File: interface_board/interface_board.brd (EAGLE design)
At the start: 65 x 56 mm, 89 parts, among them IC1 V7805-1000, IC6 LAN9512-JZX, K2 61400826021, Q1 IRLML6346TRPBF, Q6 CTS_32X25_SMD, U1 AL5812MP-13, U2 MPU-9250

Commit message: after order
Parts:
- moved LOGO1 27.6 mm to (7.61, 33.7), turned to 90 degrees
- moved C1 5.94 mm to (17.7, 12.4), turned to 0 degrees
- moved FB2 3.52 mm to (34.6, 9.66), turned to 270 degrees
- moved C41 3.29 mm to (38.1, 3.43), turned to 270 degrees
- moved U1 3.05 mm to (16.4, 16.9)
- moved C16 2.41 mm to (17.7, 13.7)
- moved R8 2.29 mm to (51.7, 5.46), turned to 90 degrees
- moved R33 1.92 mm to (34.6, 13.2), turned to 90 degrees
- moved C29 1.71 mm to (47.2, 5.46)
- moved C35 1.53 mm to (38.4, 11.2), turned to 180 degrees
- moved C32 1.42 mm to (43.1, 11.7)
- moved C27 1.42 mm to (38.4, 7.24)
- moved C28 1.42 mm to (38.4, 9.78)
- moved C39 1.42 mm to (47.2, 2.79)
- moved C40 1.42 mm to (47.2, 4.06)
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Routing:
- net 3V3A: track 82.7 -> 104.2 mm
- net +3V3: track 214.5 -> 208.0 mm, vias 9 -> 10
- net VDD18PLL: track 29.8 -> 33.3 mm
- net N$10: track 94.7 -> 98.0 mm
- net TX_P: track 63.2 -> 60.1 mm
- net N$5: track 1.68 -> 4.73 mm
- net +12V: track 70.3 -> 67.6 mm
- net +5V: track 119.2 -> 121.7 mm
- net N$9: track 85.1 -> 87.4 mm
- net XI: track 31.0 -> 32.6 mm
- net XO: track 26.5 -> 27.9 mm
- net N$43: track 7.12 -> 8.53 mm
- net NSPD_LED: track 55.8 -> 57.2 mm
- net USBD3_N: track 10.7 -> 12.0 mm
- net USBD2_N: track 7.97 -> 9.34 mm
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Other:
- outline, holes or cut-outs redrawn

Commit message: bom
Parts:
- C3: device SparkFun-Capacitors:0603-CAP -> resistor:C0402
- C42: device resistor:C0603 -> resistor:C0402
- JP1: value M20-9990446 -> SSQ-108-03-G-D
- JP2, JP3: value M20-9980346 -> M20-9980345
- JP4: value (none) -> M20-9980345
- JP6: value USB-IDMICRO -> 10118192-0001LF
- Q6: value CTS_32X25_SMD -> FA-238 25.0000MB
- R1: value 4.99K -> 4.99k
- R18, R3: value 1K -> 1k
- R2: value 100K -> 100k
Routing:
- net N$4: track 4.73 -> 4.02 mm
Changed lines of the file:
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@@
 <attribute name="NAME" x="58.9" y="25.935" size="0.6096" layer="25" font="vector" ratio="10" rot="R90"/>
 </element>
-<element name="R1" library="resistor" package="R0402" value="4.99K" x="23.008" y="18.707" smashed="yes" rot="R270">
+<element name="R1" library="resistor" package="R0402" value="4.99k" x="23.008" y="18.707" smashed="yes" rot="R270">
 <attribute name="NAME" x="23.77" y="19.342" size="0.6096" layer="25" rot="R270"/>
 <attribute name="VALUE" x="21.103" y="19.342" size="1.016" layer="27" rot="R270" display="off"/>
@@
 <attribute name="VALUE" x="17.042" y="10.505" size="1.016" layer="27" display="off"/>
 </element>
-<element name="R2" library="resistor" package="R0402" value="100K" x="16.898" y="21.312" smashed="yes" rot="R90">
+<element name="R2" library="resistor" package="R0402" value="100k" x="16.898" y="21.312" smashed="yes" rot="R90">
 <attribute name="NAME" x="17.152" y="22.963" size="0.6096" layer="25" rot="R90"/>
 <attribute name="VALUE" x="18.803" y="20.677" size="1.016" layer="27" rot="R90" display="off"/>
 </element>
-<element name="R3" library="resistor" package="R0402" value="1K" x="15.628" y="21.312" smashed="yes" rot="R270">
+<element name="R3" library="resistor" package="R0402" value="1k" x="15.628" y="21.312" smashed="yes" rot="R270">
 <attribute name="NAME" x="15.882" y="22.963" size="0.6096" layer="25" rot="R90"/>
 <attribute name="VALUE" x="13.723" y="21.947" size="1.016" layer="27" rot="R270" display="off"/>
@@
 <element name="H3" library="holes" package="2,8-PAD" value="MOUNT-PAD-ROUND2.8" x="61.5" y="3.5" smashed="yes" rot="R180"/>
 <element name="H4" library="holes" package="2,8-PAD" value="MOUNT-PAD-ROUND2.8" x="3.5" y="3.5" smashed="yes" rot="R180"/>
-<element name="JP1" library="pinhead" package="2X08" value="M20-9990446" x="17.26" y="52.5" smashed="yes" rot="MR180">
+<element name="JP1" library="pinhead" package="2X08" value="SSQ-108-03-G-D" x="17.26" y="52.5" smashed="yes" rot="MR180">
 <attribute name="NAME" x="16.6758" y="49.6552" size="0.6096" layer="26" ratio="10" rot="MR180"/>
 <attribute name="VALUE" x="12.18" y="55.675" size="1.27" layer="28" rot="MR180" display="off"/>
@@
 <attribute name="VALUE" x="18.312" y="15.628" size="1.016" layer="27" rot="R180" display="off"/>
 </element>
-<element name="R18" library="resistor" package="R0402" value="1K" x="8.536" y="25.761" smashed="yes" rot="MR180">
+<element name="R18" library="resistor" package="R0402" value="1k" x="8.536" y="25.761" smashed="yes" rot="MR180">
 <attribute name="NAME" x="5.488" y="26.015" size="0.6096" layer="26" rot="MR180"/>
 <attribute name="VALUE" x="7.901" y="27.666" size="1.016" layer="28" rot="MR180" display="off"/>
@@
 <attribute name="VALUE" x="5.227" y="18.061" size="1.016" layer="28" rot="MR90" display="off"/>
 </element>
-<element name="JP2" library="pinhead" package="2X03" value="M20-9980346" x="15.343" y="32.886" smashed="yes" rot="MR180">
+<element name="JP2" library="pinhead" package="2X03" value="M20-9980345" x="15.343" y="32.886" smashed="yes" rot="MR180">
 <attribute name="NAME" x="14.708" y="37.712" size="0.6096" layer="26" ratio="10" rot="MR180"/>
 <attribute name="VALUE" x="11.533" y="39.871" size="1.016" layer="28" rot="MR180" display="off"/>
 </element>
-<element name="JP3" library="pinhead" package="2X03" value="M20-9980346" x="33.403" y="3.936" smashed="yes" rot="MR90">
+<element name="JP3" library="pinhead" package="2X03" value="M20-9980345" x="33.403" y="3.936" smashed="yes" rot="MR90">
 <attribute name="NAME" x="36.324" y="3.301" size="0.6096" layer="26" ratio="10" rot="MR90"/>
 <attribute name="VALUE" x="26.418" y="0.126" size="1.016" layer="28" rot="MR90" display="off"/>
@@
 <attribute name="VALUE" x="36.195" y="4.064" size="0.6096" layer="27" rot="R270" display="off"/>
 </element>
-<element name="C42" library="resistor" package="C0603" value="1u" x="48.133" y="18.923" smashed="yes" rot="R270">
+<element name="C42" library="resistor" package="C0402" value="1u" x="48.133" y="18.923" smashed="yes" rot="R270">
 <attribute name="NAME" x="47.879" y="21.971" size="0.6096" layer="25" rot="R270"/>
 <attribute name="VALUE" x="44.958" y="19.685" size="0.6096" layer="27" rot="R270"/>
@@
 <attribute name="VALUE" x="26.924" y="13.97" size="0.6096" layer="27" rot="R270" display="off"/>
 </element>
-<element name="Q6" library="raspi" package="CTS_32X25" value="CTS_32X25_SMD" x="31.75" y="13.208" smashed="yes" rot="R90">
+<element name="Q6" library="raspi" package="CTS_32X25" value="FA-238 25.0000MB" x="31.75" y="13.208" smashed="yes" rot="R90">
 <attribute name="NAME" x="33.652" y="12.27" size="0.6096" layer="25" rot="R90"/>
 <attribute name="VALUE" x="33.85" y="11.508" size="0.6096" layer="27" rot="R90" display="off"/>
@@
 <attribute name="VALUE" x="31.357" y="37.465" size="0.6096" layer="27" ratio="11" display="off"/>
 </element>
-<element name="C3" library="SparkFun-Capacitors" package="0603-CAP" value="1uF" x="36.449" y="37.973" smashed="yes" rot="R180">
+<element name="C3" library="resistor" package="C0402" value="1uF" x="36.449" y="37.973" smashed="yes" rot="R180">
 <attribute name="NAME" x="36.957" y="36.957" size="0.6096" layer="25" font="vector" rot="R180"/>
 <attribute name="VALUE" x="37.465" y="39.116" size="0.6096" layer="27" font="vector" rot="R180" display="off"/>
 </element>
-<element name="JP6" library="openblw" package="USB-MICRO" value="USB-IDMICRO" x="18.796" y="1.524" smashed="yes">
+<element name="JP6" library="openblw" package="USB-MICRO" value="10118192-0001LF" x="18.796" y="1.524" smashed="yes">
 <attribute name="PROD_ID" value="CONN-09505" x="18.796" y="1.524" size="1.778" layer="27" display="off"/>
 </element>
-<element name="JP4" library="pinhead" package="2X03" value="" x="54.09" y="52.5" smashed="yes">
+<element name="JP4" library="pinhead" package="2X03" value="M20-9980345" x="54.09" y="52.5" smashed="yes">
 <attribute name="NAME" x="50.788" y="49.452" size="0.6096" layer="25" ratio="10"/>
-<attribute name="VALUE" x="50.28" y="48.055" size="1.27" layer="27"/>
+<attribute name="VALUE" x="50.28" y="48.055" size="1.27" layer="27" display="off"/>
 </element>
 <element name="LED3" library="led" package="CHIP-LED0603" value="GREEN" x="26.035" y="6.096" smashed="yes" rot="R180">
@@
 <wire x1="33.274" y1="41.402" x2="33.227" y2="41.449" width="0.2" layer="1"/>
 <wire x1="33.227" y1="41.449" x2="33.227" y2="41.986" width="0.2" layer="1"/>
-<wire x1="48.133" y1="19.773" x2="49.453" y2="19.78" width="0.2" layer="1"/>
-<wire x1="49.453" y1="19.78" x2="49.657" y2="19.573" width="0.2" layer="1"/>
+<wire x1="48.133" y1="19.573" x2="49.584" y2="19.572" width="0.2" layer="1"/>
+<wire x1="49.584" y1="19.572" x2="49.657" y2="19.573" width="0.2" layer="1"/>
 <wire x1="32.43" y1="38.783" x2="32.43" y2="37.637" width="0.2" layer="1"/>
 <wire x1="32.43" y1="37.637" x2="32.385" y2="37.592" width="0.2" layer="1"/>
@@
 <contactref element="FB3" pad="2"/>
 <via x="46.946" y="13.203" extent="1-16" drill="0.3"/>
-<wire x1="48.133" y1="18.073" x2="48.58" y2="18.012" width="0.2" layer="1"/>
+<wire x1="48.133" y1="18.273" x2="48.199" y2="18.266" width="0.2" layer="1"/>
 <wire x1="48.199" y1="16.256" x2="48.133" y2="16.444" width="0.2" layer="1"/>
-<wire x1="48.133" y1="16.444" x2="48.133" y2="18.073" width="0.2" layer="1"/>
+<wire x1="48.133" y1="16.444" x2="48.133" y2="18.273" width="0.2" layer="1"/>
 <wire x1="46.946" y1="13.203" x2="46.946" y2="15.704" width="0.2" layer="1"/>
 <wire x1="46.946" y1="15.704" x2="47.498" y2="16.256" width="0.2" layer="1"/>
@@
 <contactref element="C3" pad="2"/>
 <contactref element="U2" pad="10"/>
-<wire x1="35.599" y1="37.973" x2="36.107" y2="37.758" width="0.254" layer="1"/>
-<wire x1="36.107" y1="37.758" x2="36.068" y2="37.719" width="0.4064" layer="1"/>
-<wire x1="36.068" y1="37.719" x2="33.147" y2="37.719" width="0.4064" layer="1"/>
+<wire x1="35.799" y1="37.973" x2="35.726" y2="37.758" width="0.254" layer="1"/>
+<wire x1="35.726" y1="37.758" x2="35.687" y2="37.719" width="0.4064" layer="1"/>
+<wire x1="35.687" y1="37.719" x2="33.147" y2="37.719" width="0.4064" layer="1"/>
 <wire x1="33.147" y1="37.719" x2="32.827" y2="38.039" width="0.254" layer="1"/>
 <wire x1="32.827" y1="38.039" x2="32.827" y2="38.786" width="0.254" layer="1"/>

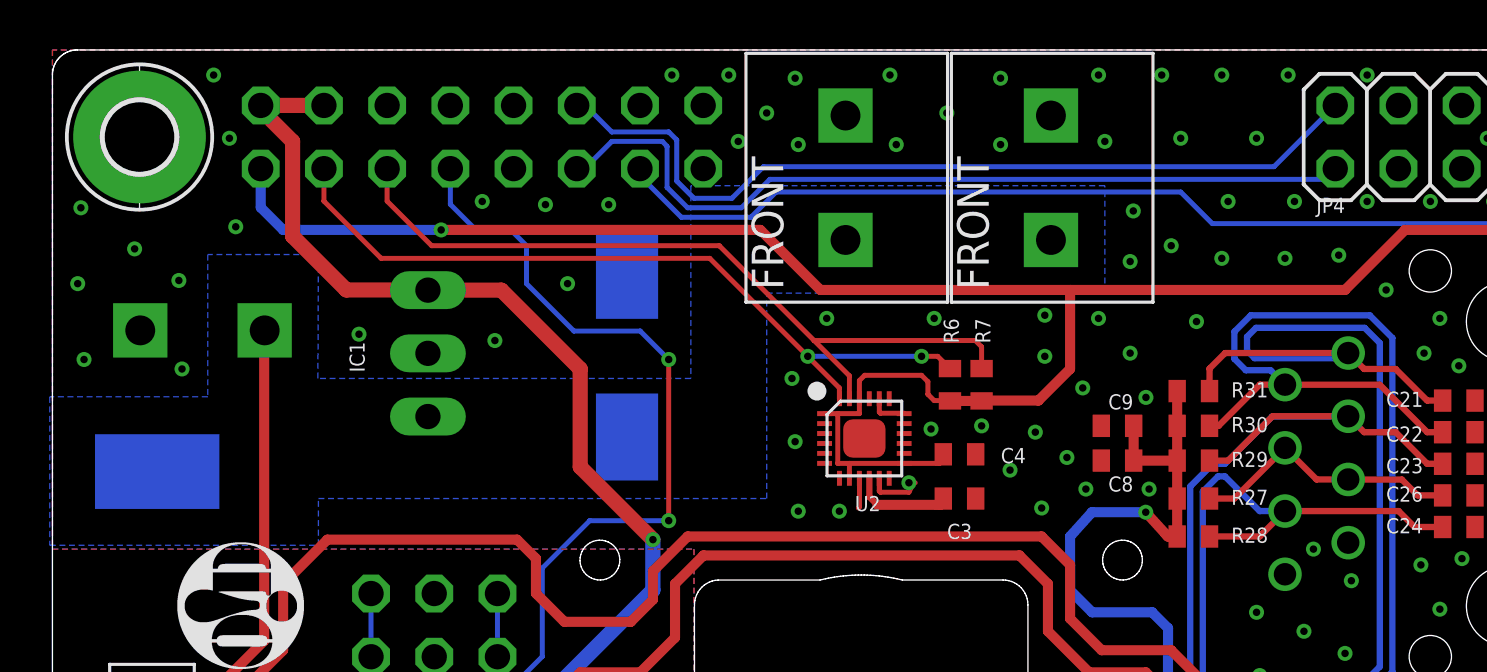
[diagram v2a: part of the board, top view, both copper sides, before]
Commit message: tune +5V
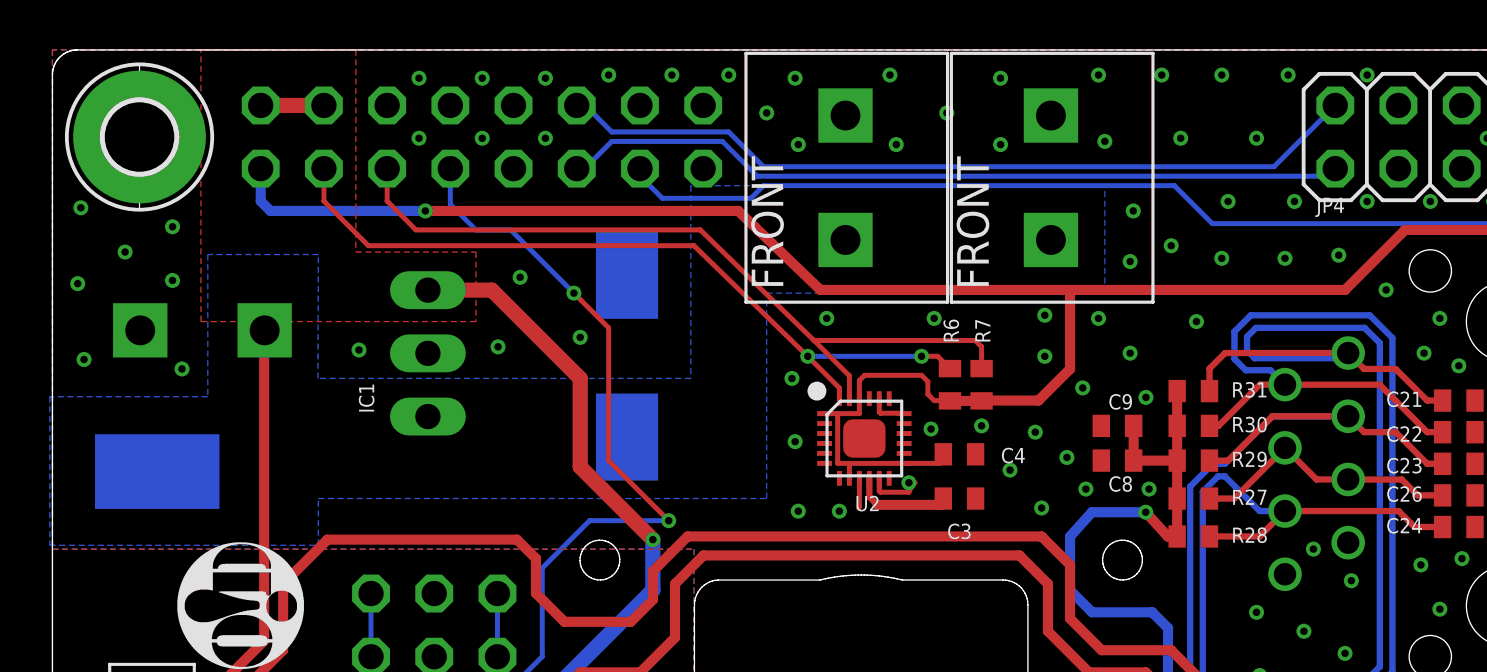
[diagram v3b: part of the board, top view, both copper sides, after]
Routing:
- net +5V: track 121.7 -> 109.3 mm
- net PWMA: track 33.7 -> 31.6 mm
- net PWMB: track 34.5 -> 32.5 mm
- net LIGHT_PWM: track 44.2 -> 42.6 mm
- net GND: vias 221 -> 223
- added copper zone on layer 1, net +5V

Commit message: before hdmi
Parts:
- removed R9: 10k, resistor:R0402
- removed U$7: 282836-2, openblw:282836-2
- added JP5: (no value), openblw:1X02
- JP1: device pinhead:2X08 -> pinhead:2X10
- R8: value 0 -> 12k
- moved JP6 56.2 mm to (37.6, 54.5), flipped to the bottom, turned to 180 degrees
- moved R8 55.1 mm to (-0.64, -11.9), turned to 0 degrees
- moved R7 39.3 mm to (21.7, 6.48)
- moved U2 38.8 mm to (18.3, 4.32)
- moved C3 38.8 mm to (22.1, 1.91)
- moved C4 38.8 mm to (22.1, 3.68)
- moved R6 38.4 mm to (23.0, 6.48)
- moved U$8 10.4 mm to (32.0, 40.4), turned to 0 degrees
- moved C17 8.86 mm to (4.09, 21.1), flipped to the top
- moved R18 5.44 mm to (4.09, 22.6), flipped to the top, turned to 0 degrees
- moved Q1 3.94 mm to (16.4, 19.9)
- moved C44 3.24 mm to (28.8, 17.4)
- moved C45 3.24 mm to (28.8, 11.8)
- moved Q6 3.24 mm to (28.8, 14.6)
- moved R19 3.24 mm to (25.9, 14.7)
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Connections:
- removed net N$10: JP1.14, R8.2
- new net N$13: JP3.2, R15.2
- net +12V: no longer U$7.CON1
- net +3V3: now also JP1.18, R8.1; no longer JP1.2, R9.2
- net GND: no longer JP3.2, R15.2, U$7.CON2
- net LAN_RUN: now also R8.2; no longer R8.1, R9.1
- net USB_D_N: now also JP5.2
- net USB_D_P: now also JP5.1
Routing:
- net N$10: track 97.6 -> 0.00 mm, vias 1 -> 0
- net +5V: track 109.3 -> 63.4 mm, vias 2 -> 5
- net TWI_SDA: track 31.4 -> 59.0 mm, vias 2 -> 3
- net N$9: track 87.4 -> 62.6 mm
- net +3V3: track 207.9 -> 183.2 mm, vias 10 -> 9
- net TWI_SCL: track 31.4 -> 56.0 mm, vias 0 -> 3
- net USB_D_P: track 46.5 -> 63.4 mm, vias 1 -> 0
- net USB_D_N: track 47.2 -> 63.5 mm, vias 1 -> 0
- net N$1: track 77.8 -> 90.1 mm
- net LIGHT_PWM: track 42.6 -> 31.2 mm
- net N$13: track 0.00 -> 11.1 mm
- net 3V3A: track 104.2 -> 96.8 mm
- net LAN_RUN: track 5.93 -> 0.00 mm, vias 1 -> 0
- net N$3: track 0.00 -> 3.67 mm, vias 0 -> 1
- net XO: track 27.9 -> 30.6 mm
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- added copper zone on layer 16, net +5V

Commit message: after hdmi
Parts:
- moved R8 54.5 mm to (51.2, 4.83), turned to 270 degrees
- moved JP4 17.8 mm to (36.3, 52.5)
- moved JP5 15.2 mm to (52.8, 48.7), turned to 180 degrees
- moved JP6 14.9 mm to (52.5, 54.5), flipped to the top
- moved ETHERNET 0.25 mm to (58.7, 39.4)
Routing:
- net PWMB: track 32.2 -> 13.6 mm
- net PWMA: track 31.4 -> 13.6 mm
- net USB_D_N: track 63.5 -> 51.0 mm, vias 0 -> 1
- net USB_D_P: track 63.4 -> 51.0 mm, vias 0 -> 1
- net LAN_RUN: track 0.00 -> 4.45 mm, vias 0 -> 1
- net TX_N: track 59.8 -> 61.0 mm
- net +3V3: track 183.2 -> 183.9 mm, vias 9 -> 10
- net TX_P: track 60.1 -> 60.7 mm
- net GND: vias 213 -> 211
- net +5V: vias 5 -> 9

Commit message: before autorouter
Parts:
- added C5, C6: 22u, resistor:C0603
- added L1: SRN4018-100M(10u), openblw:BOURNS-SRN4018
- C16: value 1u -> 10u; device resistor:C0402 -> resistor:C0603
- moved C16 26.4 mm to (16.1, 39.2), turned to 0 degrees
- moved LOGO1 4.19 mm to (7.61, 37.9)
- moved C2 1.91 mm to (21.2, 43.7)
- moved C1 0.89 mm to (17.7, 12.4)
- moved C32 0.51 mm to (43.6, 11.7)
- moved C33 0.51 mm to (42.0, 11.7)
- moved U$8 0.50 mm to (32.5, 40.4)
- moved C22 0.38 mm to (56.5, 40.3)
- moved C23 0.38 mm to (56.5, 39.0)
- moved C24 0.38 mm to (56.5, 36.4)
- moved C26 0.38 mm to (56.5, 37.7)
- moved C34 0.38 mm to (40.4, 11.7)
- moved C8 0.38 mm to (42.8, 39.1)
- moved C9 0.38 mm to (42.8, 40.5)
- moved ETHERNET 0.38 mm to (58.7, 39.0)
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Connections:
- new net N$10: C5.1, IC1.OUT, L1.P$2
- net +12V: now also U$4.CON1; no longer U$4.CON2
- net +5V: now also C6.1, L1.P$1; no longer IC1.OUT
- net GND: now also C5.2, C6.2, JP1.19, U$4.CON2; no longer U$4.CON1
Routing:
- net +5V: track 63.4 -> 55.3 mm
- net +12V: track 66.7 -> 68.0 mm
- net NLNKA_LED: track 64.3 -> 63.0 mm
- net 3V3A: track 96.8 -> 98.0 mm
- net NSPD_LED: track 57.3 -> 56.4 mm
- net LIGHT_PWM: track 31.2 -> 30.3 mm
- net +3V3: track 183.9 -> 183.3 mm
- net GND: vias 211 -> 205
- added copper zone on layer 1, net N$10
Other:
- board text added: "GND"
- board text added: "Rev.0.5"
- board text removed: "Rev.0.4"
